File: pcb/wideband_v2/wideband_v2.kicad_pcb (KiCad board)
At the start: 2 copper layers, 50 x 40 mm, 103 parts, among them J1 DISPLAY, J2 GPIO, J3 LSU, J4 Tag connect, J5 USB, Q1 BTS3028, SW1 SW_Push, U1 DAC5571IDBVR, U10 XC6206P332MR, U2 L7805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

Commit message: BTS3028 => WSF60N06 | AD8628 => OPA388IDR
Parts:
- Q1: value BTS3028 -> WSF60N06
- U8: value AD8628 -> OPA388IDR
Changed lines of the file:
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@@
     (descr "TO-252 / DPAK SMD package, http://www.infineon.com/cms/en/product/packages/PG-TO252/PG-TO252-3-1/")
     (tags "DPAK TO-252 DPAK-3 TO-252-3 SOT-428")
-    (property "LCSC" "C112639")
+    (property "LCSC" "C148432")
     (property "Sheetfile" "wideband.kicad_sch")
     (property "Sheetname" "Wideband")
@@
       (effects (font (size 1 1) (thickness 0.15)))
     )
-    (fp_text value "BTS3028" (at 0 4.5) (layer "F.Fab")
+    (fp_text value "WSF60N06" (at 0 4.5) (layer "F.Fab")
       (effects (font (size 1 1) (thickness 0.15)))
     )
@@
     (descr "TSOT, 5 Pin (https://www.jedec.org/sites/default/files/docs/MO-193D.pdf variant AB), generated with kicad-footprint-generator ipc_gullwing_generator.py")
     (tags "TSOT TO_SOT_SMD")
-    (property "LCSC" "C29309")
+    (property "LCSC" "C154118")
     (property "Sheetfile" "wideband.kicad_sch")
     (property "Sheetname" "Wideband")
@@
       (effects (font (size 1 1) (thickness 0.15)))
     )
-    (fp_text value "AD8628" (at 0 2.4 90) (layer "F.Fab")
+    (fp_text value "OPA388IDR" (at 0 2.4 90) (layer "F.Fab")
       (effects (font (size 1 1) (thickness 0.15)))
     )
@@
     (pts (xy 103.5 38) (xy 103.5 78))
     (height 1)
-    (gr_text "40.0000 mm" (at 101.35 58 90) (layer "Dwgs.User")
+    (gr_text "40,0000 mm" (at 101.35 58 90) (layer "Dwgs.User")
       (effects (font (size 1 1) (thickness 0.15)))
     )
@@
     (pts (xy 154 38) (xy 104 38))
     (height 1.5)
-    (gr_text "50.0000 mm" (at 129 35.35) (layer "Dwgs.User")
+    (gr_text "50,0000 mm" (at 129 35.35) (layer "Dwgs.User")
       (effects (font (size 1 1) (thickness 0.15)))
     )

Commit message: tune tracks/vias
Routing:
- net Net-(C26-Pad2): track 14.3 -> 13.3 mm

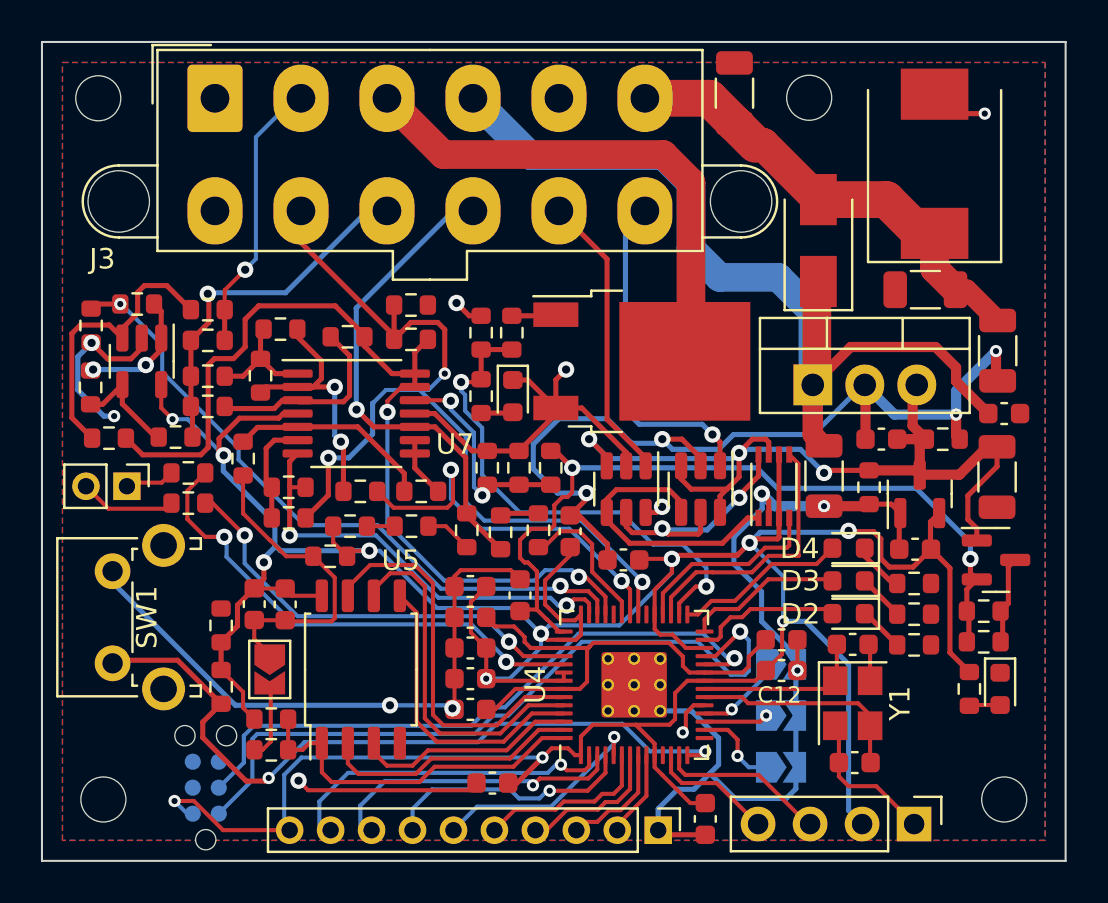
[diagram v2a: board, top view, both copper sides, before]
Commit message: add CAN controller
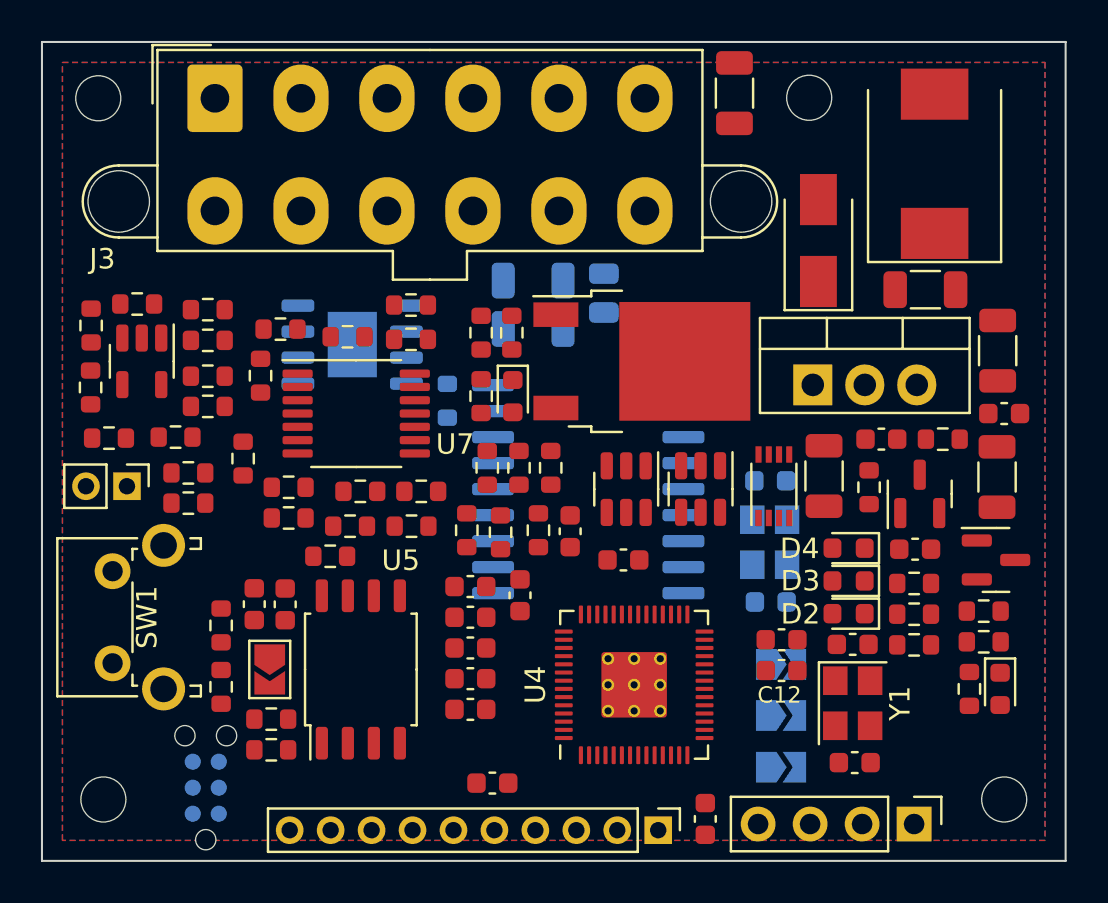
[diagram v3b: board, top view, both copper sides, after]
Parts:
- added C36: 30pF, Capacitor_SMD:C_0603_1608Metric, B.Cu at (139.6, 65.4)
- added C37: 30pF, Capacitor_SMD:C_0603_1608Metric, B.Cu at (139.6, 59.4)
- added C38: 4.7nF, Capacitor_SMD:C_0805_2012Metric, B.Cu at (131.4, 50.3)
- added R35: 10k, Resistor_SMD:R_0603_1608Metric, B.Cu at (123.8, 55.5)
- added R36: R_Small, Resistor_SMD:R_1206_3216Metric, B.Cu at (128.0, 52.0)
- added R37: R_Small, Resistor_SMD:R_1206_3216Metric, B.Cu at (128.0, 49.7)
- added U11: MCP2515-xSO, Package_SO:SOIC-18W_7.5x11.6mm_P1.27mm, B.Cu at (130.7, 59.8)
- added U12: TJA1042T3118, Package_SO:HTSOP-8-1EP_3.9x4.9mm_P1.27mm_EP2.4x3.2mm, B.Cu at (119.2, 52.8)
- added Y2: 12MHz, Crystal:Crystal_SMD_3225-4Pin_3.2x2.5mm, B.Cu at (139.5, 62.4)
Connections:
- J3 pad 11: /V0 -> CAN+
- J3 pad 12: /V1 -> CAN-
- J3 pad 5: unconnected-(J3-Pad5) -> /V0
- J3 pad 7: GND -> /V1
- U4 pad 11: unconnected-(U4-Pad11) -> /GPIO8
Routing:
- net GND: track 192.4 -> 0.00 mm, vias 17 -> 0
- net +3V3: track 179.6 -> 0.00 mm, vias 12 -> 0
- net /Vm: track 45.9 -> 0.00 mm, vias 2 -> 0
- net /LSU_Heater+: track 45.8 -> 0.00 mm
- net /LSU_Vm: track 44.9 -> 0.00 mm, vias 3 -> 0
- net +5V: track 44.3 -> 0.00 mm, vias 3 -> 0
- net VDDA: track 39.4 -> 0.00 mm, vias 2 -> 0
- net /MODE_CHG: track 36.4 -> 0.00 mm, vias 2 -> 0
- net /SYS_SWDIO: track 35.6 -> 0.00 mm, vias 1 -> 0
- net /Ip_sense: track 32.7 -> 0.00 mm, vias 2 -> 0
- net /SYS_SWCLK: track 31.2 -> 0.00 mm, vias 1 -> 0
- net /LSU_Heater-: track 25.4 -> 0.00 mm
- net /heater_pwm: track 24.9 -> 0.00 mm, vias 2 -> 0
- net Net-(R6-Pad2): track 24.5 -> 0.00 mm, vias 2 -> 0
- net /LSU_Un: track 24.1 -> 0.00 mm, vias 1 -> 0
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
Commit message: trace external i/o
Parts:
- removed C10: 100nF, Capacitor_SMD:C_0603_1608Metric
- moved U4 0.80 mm to (133.0, 68.6)
- moved C19 0.05 mm to (127.3, 65.0)
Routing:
- net +3V3: track 0.00 -> 46.8 mm, vias 0 -> 11
- net /LSU_Rtrim: track 0.00 -> 19.8 mm, vias 0 -> 1
- net Net-(R7-Pad1): track 0.00 -> 18.3 mm
- net GND: track 0.00 -> 17.0 mm, vias 0 -> 7
- net /GPIO0: track 0.00 -> 15.0 mm
- net Net-(U4-Pad55): track 0.00 -> 13.5 mm
- net /GPIO1: track 0.00 -> 13.5 mm
- net +1V1: track 0.00 -> 12.1 mm
- net Net-(U4-Pad54): track 0.00 -> 12.1 mm
- net /GPIO2: track 0.00 -> 12.0 mm
- net Net-(R19-Pad1): track 0.00 -> 11.2 mm, vias 0 -> 3
- net /GPIO3: track 0.00 -> 11.2 mm
- net /GPIO4: track 0.00 -> 9.62 mm
- net /LSU_Vm: track 0.00 -> 9.14 mm
- net /OLED_SCL: track 0.00 -> 8.52 mm
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- added copper zone on In2.Cu, net +3V3
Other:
- copper layers 2 -> 4

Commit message: Routing
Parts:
- R36, R37: value R_Small -> 30R
- moved C38 13.3 mm to (118.5, 53.7)
- moved U12 9.86 mm to (128.8, 51.0), turned to 180 degrees
- moved R37 6.85 mm to (121.8, 52.7)
- moved R36 6.46 mm to (121.8, 50.0), turned to 0 degrees
- moved U11 2.42 mm to (133.1, 59.8)
- moved Y2 2.26 mm to (141.7, 63.0)
- moved C37 2.26 mm to (141.8, 60.0)
- moved C36 2.26 mm to (141.8, 66.0)
- moved R35 2.01 mm to (125.8, 55.3)
- moved C13 0.78 mm to (131.8, 62.8)
- moved C17 0.23 mm to (143.6, 67.7)
- moved C14 0.22 mm to (129.6, 61.8)
- moved Y1 0.20 mm to (143.6, 70.5)
- moved R30 0.16 mm to (128.1, 61.8)
- moved C4 0.15 mm to (142.3, 59.2)
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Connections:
- U11 pad 15: /GPIO3 -> /GPIO2
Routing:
- net GND: track 17.0 -> 140.9 mm, vias 7 -> 25
- net +5V: track 0.00 -> 51.4 mm, vias 0 -> 3
- net /LSU_Heater+: track 0.00 -> 45.3 mm
- net VDDA: track 2.31 -> 39.7 mm, vias 0 -> 3
- net /LSU_Vm: track 9.14 -> 46.2 mm, vias 0 -> 3
- net /V1: track 0.00 -> 37.0 mm
- net /Vm: track 5.80 -> 42.6 mm, vias 0 -> 2
- net /SYS_SWDIO: track 0.00 -> 32.1 mm, vias 0 -> 2
- net /Ip_sense: track 1.52 -> 33.6 mm, vias 0 -> 2
- net /SYS_SWCLK: track 0.00 -> 31.0 mm, vias 0 -> 2
- net +3V3: track 46.8 -> 76.8 mm, vias 11 -> 16
- net /MODE_CHG: track 7.40 -> 37.0 mm, vias 0 -> 2
- net /LSU_Heater-: track 0.00 -> 25.8 mm
- net 12V_RAW: track 0.00 -> 22.9 mm
- net /GPIO8: track 0.00 -> 22.9 mm, vias 0 -> 1
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- added copper zone on In1.Cu, net GND
- removed copper zone on B.Cu, net GND
- removed copper zone on F.Cu, net GND
